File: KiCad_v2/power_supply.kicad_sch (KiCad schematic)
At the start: 32 parts, among them U1 LT8582EDKD-PBF, U6 MCP73871, U7 LM3940IMP-3.3

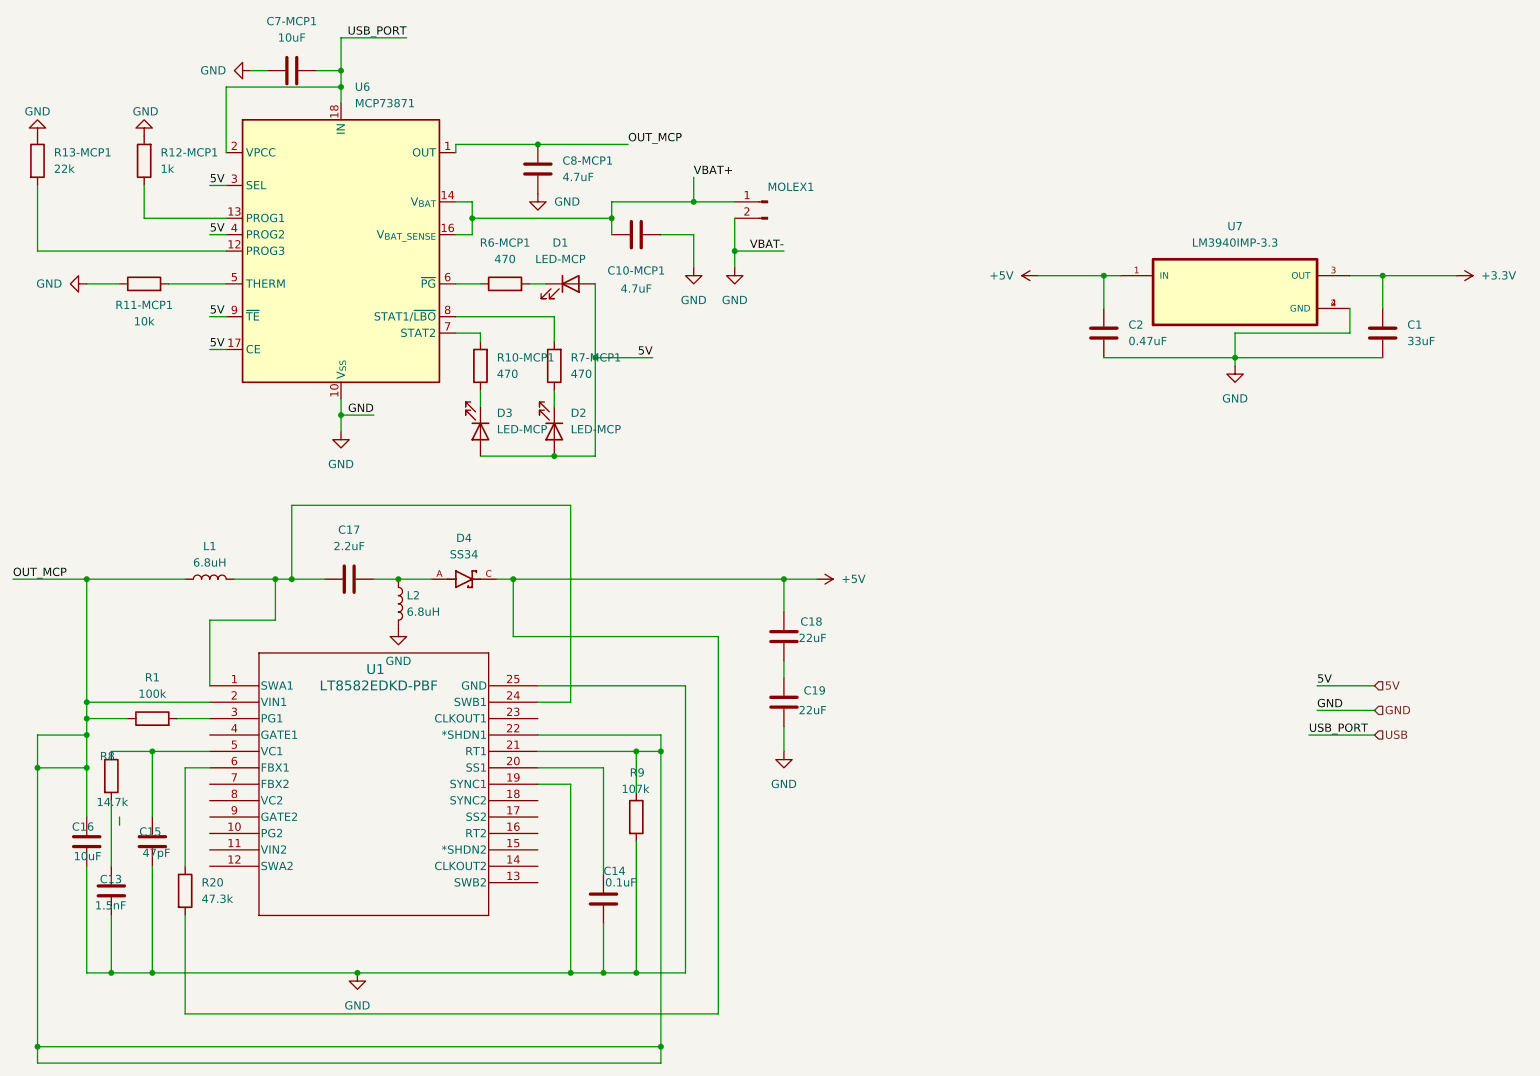
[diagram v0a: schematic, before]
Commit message: feat: comienzo rooteo y perfeccionar esquematico
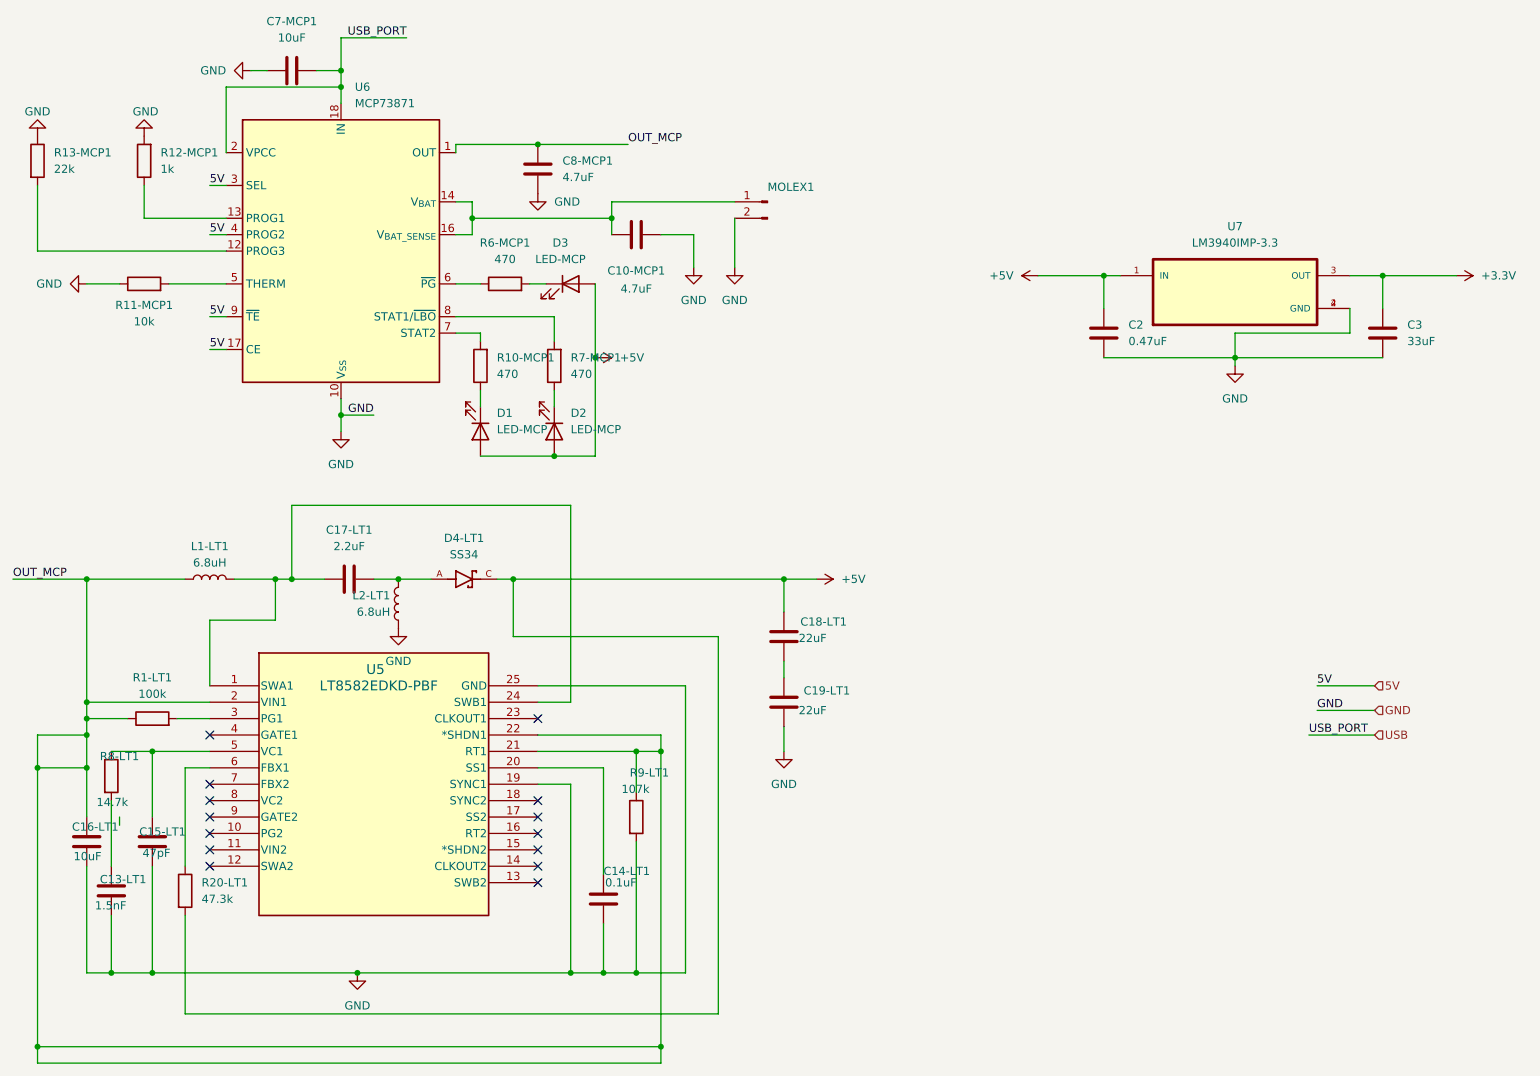
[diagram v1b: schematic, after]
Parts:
- renumbered C13 to C13-LT1, C14 to C14-LT1, C15 to C15-LT1, C16 to C16-LT1, C17 to C17-LT1, C18 to C18-LT1, C19 to C19-LT1, C1 to C3, D3 to D1, D1 to D3, D4 to D4-LT1, L1 to L1-LT1, L2 to L2-LT1, R1 to R1-LT1, R20 to R20-LT1, R8 to R8-LT1, R9 to R9-LT1, U1 to U5
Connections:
- net +5V: now also D1.2 (A), D2.2 (A), D3.2 (A)
- net 5V: no longer D1.2 (A), D2.2 (A), D3.2 (A)
- net VBAT+: no longer names the net of C10-MCP1.1, MOLEX1.1 (Pin_1), U6.14 (V_{BAT}), U6.15 (V_{BAT}), U6.16 (V_{BAT_SENSE})
- no-connect marks 0 -> 14
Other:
- moved on the sheet: L2-LT1

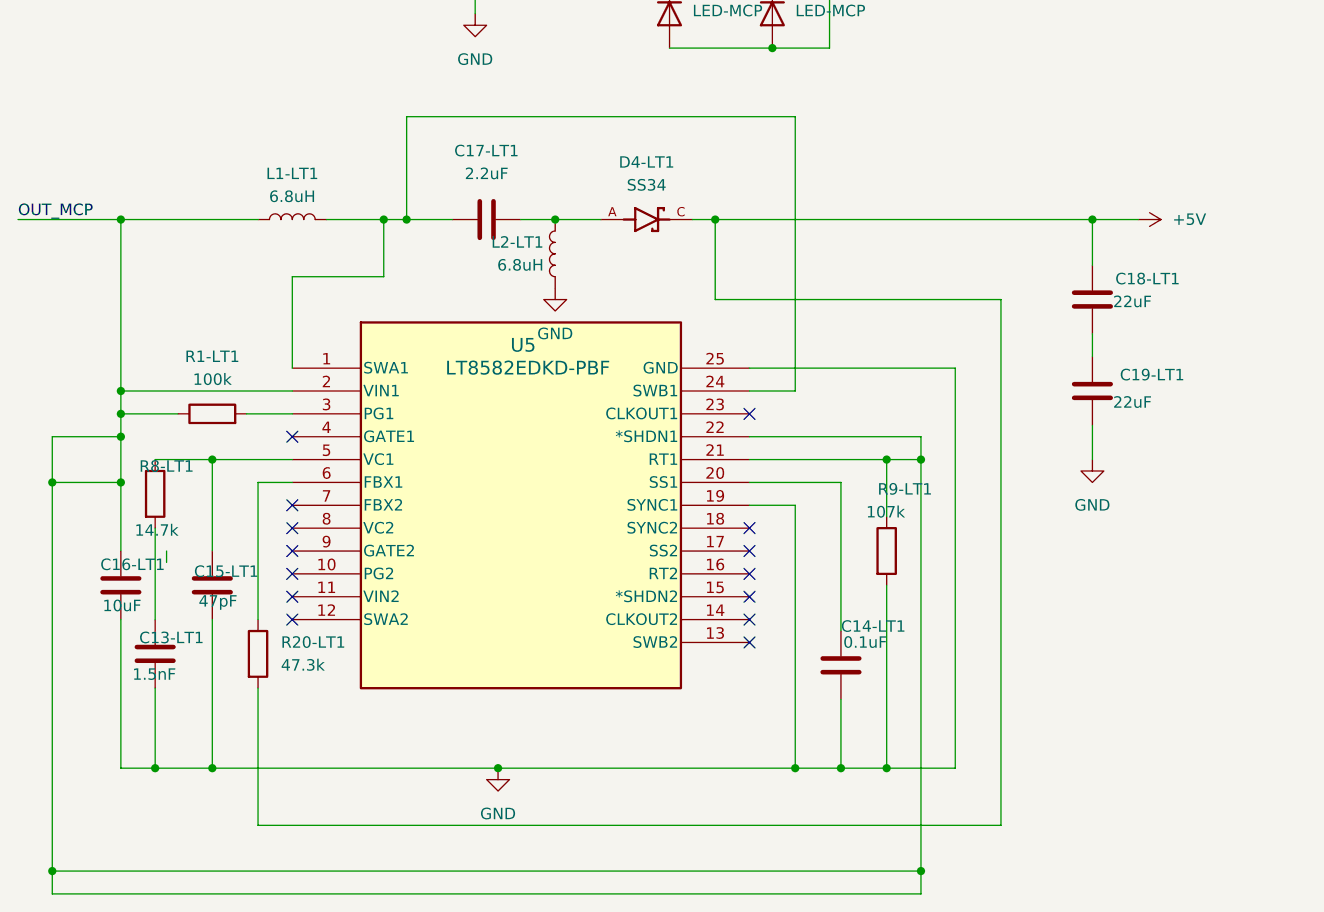
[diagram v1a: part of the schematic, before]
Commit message: feat: sigue rooteo y correccion de valores de resistencias
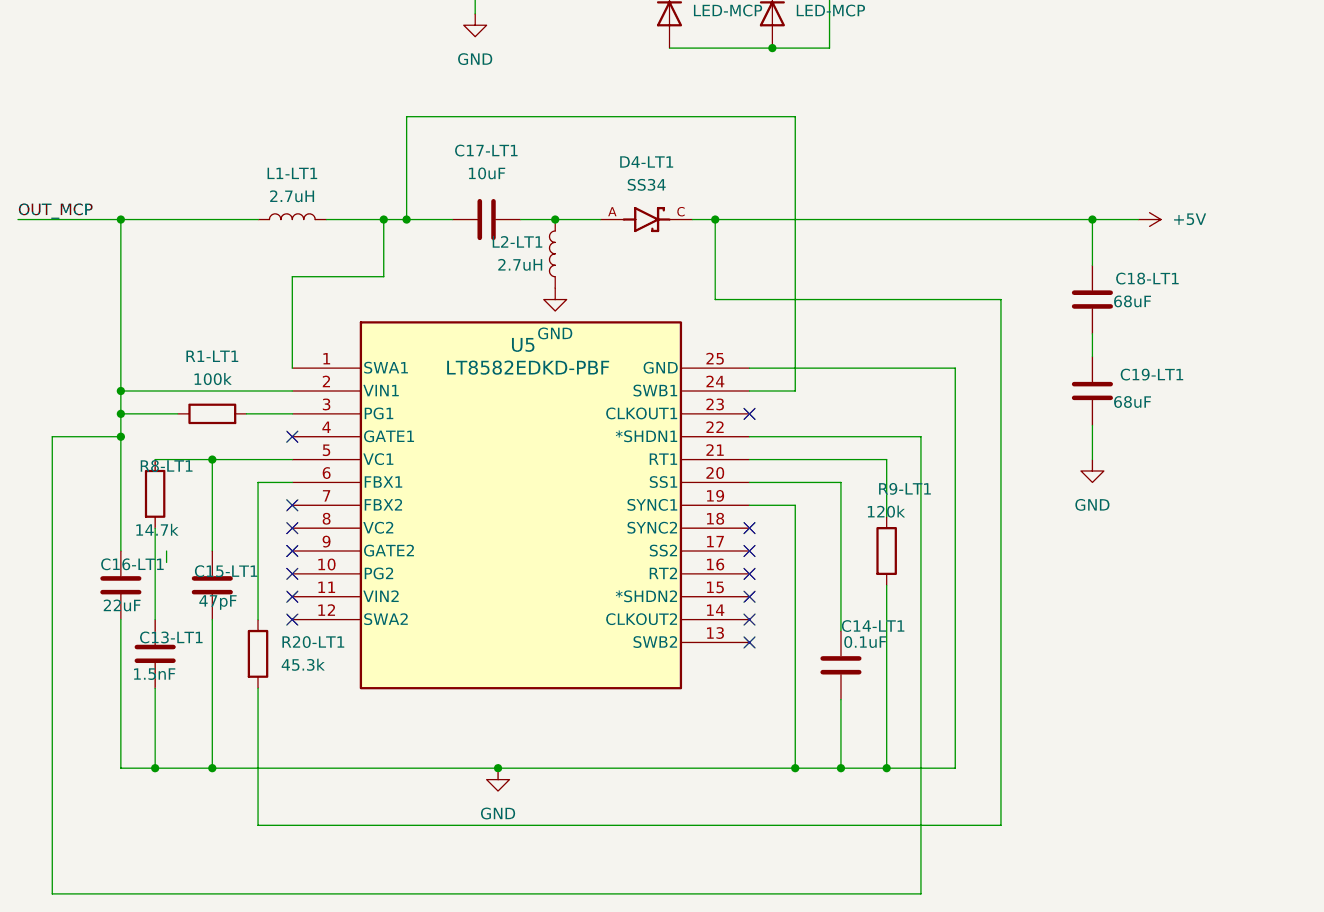
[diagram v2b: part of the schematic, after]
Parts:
- C16-LT1: value 10uF -> 22uF
- C17-LT1: value 2.2uF -> 10uF
- C18-LT1, C19-LT1: value 22uF -> 68uF
- L1-LT1, L2-LT1: value 6.8uH -> 2.7uH
- MOLEX1: footprint Connector_PinHeader_2.54mm:PinHeader_1x02_P2.54mm_Vertical -> Connector_Molex:Molex_KK-254_AE-6410-02A_1x02_P2.54mm_Vertical
- R20-LT1: value 47.3k -> 45.3k
- R9-LT1: value 107k -> 120k
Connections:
- net OUT_MCP: no longer R9-LT1.1, U5.21 (RT1)
- new net: R9-LT1.1, U5.21 (RT1)
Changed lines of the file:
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@@
 	)
 	(junction
-		(at 123.19 135.89)
-		(diameter 0)
-		(color 0 0 0 0)
-	)
-	(junction
 		(at 38.1 130.81)
 		(diameter 0)
@@
 	)
 	(junction
-		(at 127 181.61)
-		(diameter 0)
-		(color 0 0 0 0)
-	)
-	(junction
 		(at 215.9 74.93)
 		(diameter 0)
@@
 	)
 	(junction
-		(at 38.1 138.43)
-		(diameter 0)
-		(color 0 0 0 0)
-	)
-	(junction
 		(at 48.26 170.18)
 		(diameter 0)
@@
 	)
 	(junction
-		(at 30.48 138.43)
-		(diameter 0)
-		(color 0 0 0 0)
-	)
-	(junction
 		(at 107.95 41.91)
 		(diameter 0)
@@
 	)
 	(junction
-		(at 127 135.89)
-		(diameter 0)
-		(color 0 0 0 0)
-	)
-	(junction
 		(at 48.26 135.89)
 		(diameter 0)
@@
 	)
 	(junction
-		(at 30.48 181.61)
-		(diameter 0)
-		(color 0 0 0 0)
-	)
-	(junction
 		(at 116.84 74.93)
 		(diameter 0)
@@
 	(wire
 		(pts
-			(xy 38.1 138.43) (xy 38.1 146.05)
-		)
-		(stroke
-			(width 0)
-			(type default)
-		)
-	)
-	(wire
-		(pts
 			(xy 107.95 140.97) (xy 113.03 140.97)
 		)
@@
 	(wire
 		(pts
-			(xy 30.48 138.43) (xy 30.48 181.61)
-		)
-		(stroke
-			(width 0)
-			(type default)
-		)
-	)
-	(wire
-		(pts
 			(xy 107.95 135.89) (xy 123.19 135.89)
 		)
@@
 	(wire
 		(pts
-			(xy 30.48 138.43) (xy 38.1 138.43)
-		)
-		(stroke
-			(width 0)
-			(type default)
-		)
-	)
-	(wire
-		(pts
 			(xy 99.06 71.12) (xy 99.06 72.39)
 		)
@@
 	(wire
 		(pts
-			(xy 123.19 135.89) (xy 127 135.89)
-		)
-		(stroke
-			(width 0)
-			(type default)
-		)
-	)
-	(wire
-		(pts
 			(xy 41.91 143.51) (xy 41.91 153.67)
 		)
@@
 	(wire
 		(pts
-			(xy 127 135.89) (xy 127 181.61)
-		)
-		(stroke
-			(width 0)
-			(type default)
-		)
-	)
-	(wire
-		(pts
 			(xy 46.99 48.26) (xy 46.99 53.34)
 		)
@@
 	(wire
 		(pts
-			(xy 30.48 133.35) (xy 30.48 138.43)
-		)
-		(stroke
-			(width 0)
-			(type default)
-		)
-	)
-	(wire
-		(pts
 			(xy 38.1 130.81) (xy 44.45 130.81)
 		)
@@
 	(wire
 		(pts
-			(xy 127 181.61) (xy 127 184.15)
+			(xy 127 133.35) (xy 127 184.15)
 		)
 		(stroke
@@
 	(wire
 		(pts
-			(xy 127 181.61) (xy 30.48 181.61)
-		)
-		(stroke
-			(width 0)
-			(type default)
-		)
-	)
-	(wire
-		(pts
 			(xy 77.47 33.02) (xy 77.47 35.56)
 		)
@@
 	(wire
 		(pts
-			(xy 30.48 184.15) (xy 30.48 181.61)
+			(xy 30.48 133.35) (xy 30.48 184.15)
 		)
 		(stroke
@@
 	(wire
 		(pts
-			(xy 127 133.35) (xy 127 135.89)
-		)
-		(stroke
-			(width 0)
-			(type default)
-		)
-	)
-	(wire
-		(pts
 			(xy 53.34 176.53) (xy 135.89 176.53)
 		)
@@
 	(wire
 		(pts
-			(xy 38.1 133.35) (xy 38.1 138.43)
+			(xy 38.1 133.35) (xy 38.1 146.05)
 		)
 		(stroke
@@
 			)
 		)
-		(property "Value" "107k"
+		(property "Value" "120k"
 			(at 120.904 141.732 0)
 			(effects
@@
 			)
 		)
-		(property "Footprint" "Connector_PinHeader_2.54mm:PinHeader_1x02_P2.54mm_Vertical"
+		(property "Footprint" "Connector_Molex:Molex_KK-254_AE-6410-02A_1x02_P2.54mm_Vertical"
 			(at 143.51 50.8 0)
 			(effects
@@
 			)
 		)
-		(property "Value" "6.8uH"
+		(property "Value" "2.7uH"
 			(at 57.15 106.68 90)
 			(effects
@@
 			)
 		)
-		(property "Value" "47.3k"
+		(property "Value" "45.3k"
 			(at 55.88 158.7499 0)
 			(effects
@@
 			)
 		)
-		(property "Value" "22uF"
+		(property "Value" "68uF"
 			(at 148.336 129.54 0)
 			(effects
@@
 			)
 		)
-		(property "Value" "2.2uF"
+		(property "Value" "10uF"
 			(at 78.74 104.14 90)
 			(effects
@@
 			)
 		)
-		(property "Value" "10uF"
+		(property "Value" "22uF"
 			(at 36.068 152.146 0)
 			(effects
@@
 			)
 		)
-		(property "Value" "22uF"
+		(property "Value" "68uF"
 			(at 148.336 118.364 0)
 			(effects
@@
 			)
 		)
-		(property "Value" "6.8uH"
+		(property "Value" "2.7uH"
 			(at 85.09 114.2999 0)
 			(effects
